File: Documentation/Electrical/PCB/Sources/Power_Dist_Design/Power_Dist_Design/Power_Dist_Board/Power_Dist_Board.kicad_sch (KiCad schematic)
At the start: 25 parts, among them J1 Battery Connector, J2 5V Connector, J3 3.3V Connector, U1 TPS565201, U2 TPS565201

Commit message: Added fuses to pcb
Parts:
- added F1, F2, F3: Fuse, Fuse:Fuse_1206_3216Metric_Pad1.42x1.75mm_HandSolder, symbol Device:Fuse
- added J2: 12V Connector, Connector_Phoenix_MSTB:PhoenixContact_MSTBVA_2,5_2-G-5,08_1x02_P5.08mm_Vertical, symbol Connector:Conn_01x02_Female
- added SW1: Emergency Stop, Connector_Phoenix_GMSTB:PhoenixContact_GMSTBVA_2,5_2-G_1x02_P7.50mm_Vertical, symbol Switch:SW_SPST
- renumbered J2 to J3, J3 to J4
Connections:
- net +3.3V: now also F2.1; no longer C2.1, C5.1, L2.1, R3.2
- net +5V: now also F1.1; no longer C1.1, C3.1, L1.1, R4.2
- net GND: now also J2.2 (Pin_2)
- net vin: now also F3.1
- new net: F3.2, SW1.1 (A)
- new net +12V: J2.1 (Pin_1), SW1.2 (B)
- new net vout1: C1.1, C3.1, F1.2, L1.1, R4.2
- new net vout2: C2.1, C5.1, F2.2, L2.1, R3.2
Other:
- moved on the sheet: J3, J4

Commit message: Added to distribution board
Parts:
- removed J2: 12V Connector, Connector_Phoenix_MSTB:PhoenixContact_MSTBVA_2,5_2-G-5,08_1x02_P5.08mm_Vertical, symbol Connector:Conn_01x02_Female
- added D1, D2, D3: LED, LED_SMD:LED_1206_3216Metric_Pad1.42x1.75mm_HandSolder, symbol Device:LED
- added D4, D5, D6, D7, D8, D9: D, RB070MM:DIO_RB051MM_ROM-M, symbol Device:D
- added M1, M2, M3, M4, M5, M6: Motor_DC, Power_Dist:Molex_Screw_Term_0397730002, symbol Motor:Motor_DC
- added R1, R2, R3: 10k, Resistor_SMD:R_1206_3216Metric_Pad1.30x1.75mm_HandSolder, symbol Device:R_US
- J1: footprint Connector_Phoenix_MSTB:PhoenixContact_MSTBVA_2,5_2-G-5,08_1x02_P5.08mm_Vertical -> Power_Dist:Molex_Screw_Term_0397730002
- SW1: footprint Connector_Phoenix_GMSTB:PhoenixContact_GMSTBVA_2,5_2-G_1x02_P7.50mm_Vertical -> Power_Dist:Molex_Screw_Term_0397730002
- renumbered J3 to J2, J4 to J3, R1 to R4, R2 to R5, R3 to R6, R4 to R7, R5 to R8, R6 to R9
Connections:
- net +12V: now also D4.1 (K), D5.1 (K), D6.1 (K), D7.1 (K), D8.1 (K), D9.1 (K), M1.1 (+), M2.1 (+), M3.1 (+), M4.1 (+), M5.1 (+), M6.1 (+)
- net +3.3V: now also D2.1 (K)
- net +5V: now also D1.1 (K)
- net GND: now also D4.2 (A), D5.2 (A), D6.2 (A), D7.2 (A), D8.2 (A), D9.2 (A), M1.2 (-), M2.2 (-), M3.2 (-), M4.2 (-), M5.2 (-), M6.2 (-)
- net vin: now also R3.1
- net vout1: now also R1.1
- net vout2: now also R2.1
- net at F3.2, SW1.1 (A): now also D3.1 (K)
- new net: D3.2 (A), R3.2
- new net: D2.2 (A), R2.2
- new net: D1.2 (A), R1.2
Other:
- note added: "Motors with Diode Protection"
- moved on the sheet: F1, F2, F3, J2, J3, SW1

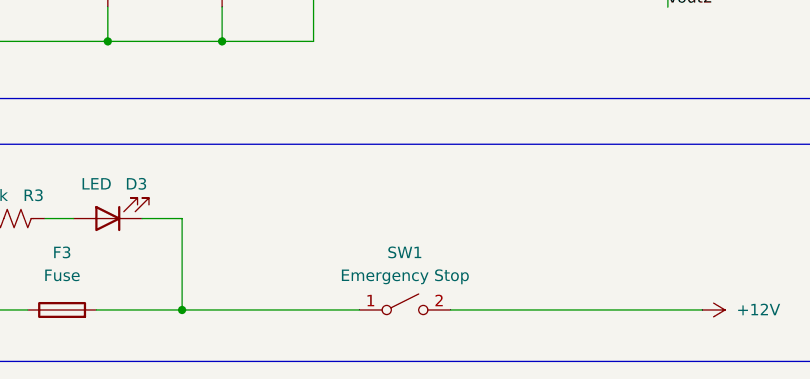
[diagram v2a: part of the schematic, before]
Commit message: Added to power distribution pcb layout
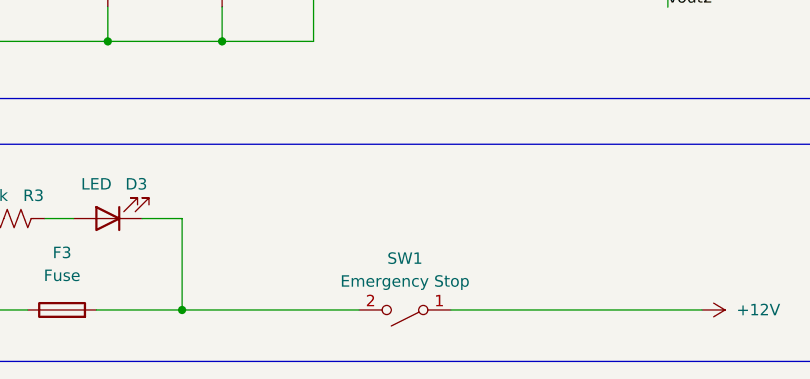
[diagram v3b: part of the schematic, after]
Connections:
- net +12V: now also SW1.1 (A); no longer SW1.2 (B)
- net at D3.1 (K), F3.2: now also SW1.2 (B); no longer SW1.1 (A)
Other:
- moved on the sheet: SW1
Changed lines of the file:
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@@
     (pin "1")
   )
-  (symbol (lib_id "Switch:SW_SPST") (at 95.25 180.975 0) (unit 1)
+  (symbol (lib_id "Switch:SW_SPST") (at 95.25 180.975 180) (unit 1)
     (in_bom yes) (on_board yes) (fields_autoplaced)
-    (property "Reference" "SW1" (id 0) (at 95.25 174.625 0))
-    (property "Value" "Emergency Stop" (id 1) (at 95.25 177.165 0))
+    (property "Reference" "SW1" (id 0) (at 95.25 175.26 0))
+    (property "Value" "Emergency Stop" (id 1) (at 95.25 177.8 0))
     (property "Footprint" "Power_Dist:Molex_Screw_Term_0397730002" (id 2) (at 95.25 180.975 0)
       (effects (font (size 1.27 1.27)) hide)
